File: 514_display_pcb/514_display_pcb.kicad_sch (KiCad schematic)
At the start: 9 parts

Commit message: Initial commit from workspace
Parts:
- U?: footprint XIAO_ESP32C3:xiao_esp32c3 -> RF_Module:MCU_Seeed_ESP32C3
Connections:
- net at Lipo?.1 (+): now also U?.1 (VI), U?.3 (VIN1+)
- net at D?.2 (GND): now also Brd?.1 (GND), SW?.1, U?.13 (GND)
- net at D?.3 (VDD): now also Brd?.2 (VCC), U?.12 (VCC_3V3)
- net at D?.4 (DIN): now also U?.2 (D1)
- net at SW?.2: now also U?.7 (D6)
- net at U?.5 (VOUT1-): now also U?.8 (GND)
- net at U?.7 (VOUT1+): now also U?.9 (COM)
- net at U?.5 (D4): now also Brd?.4 (SDA)
- net at U?.6 (D5): now also Brd?.3 (SCL)
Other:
- moved on the sheet: D?, SW?, U?

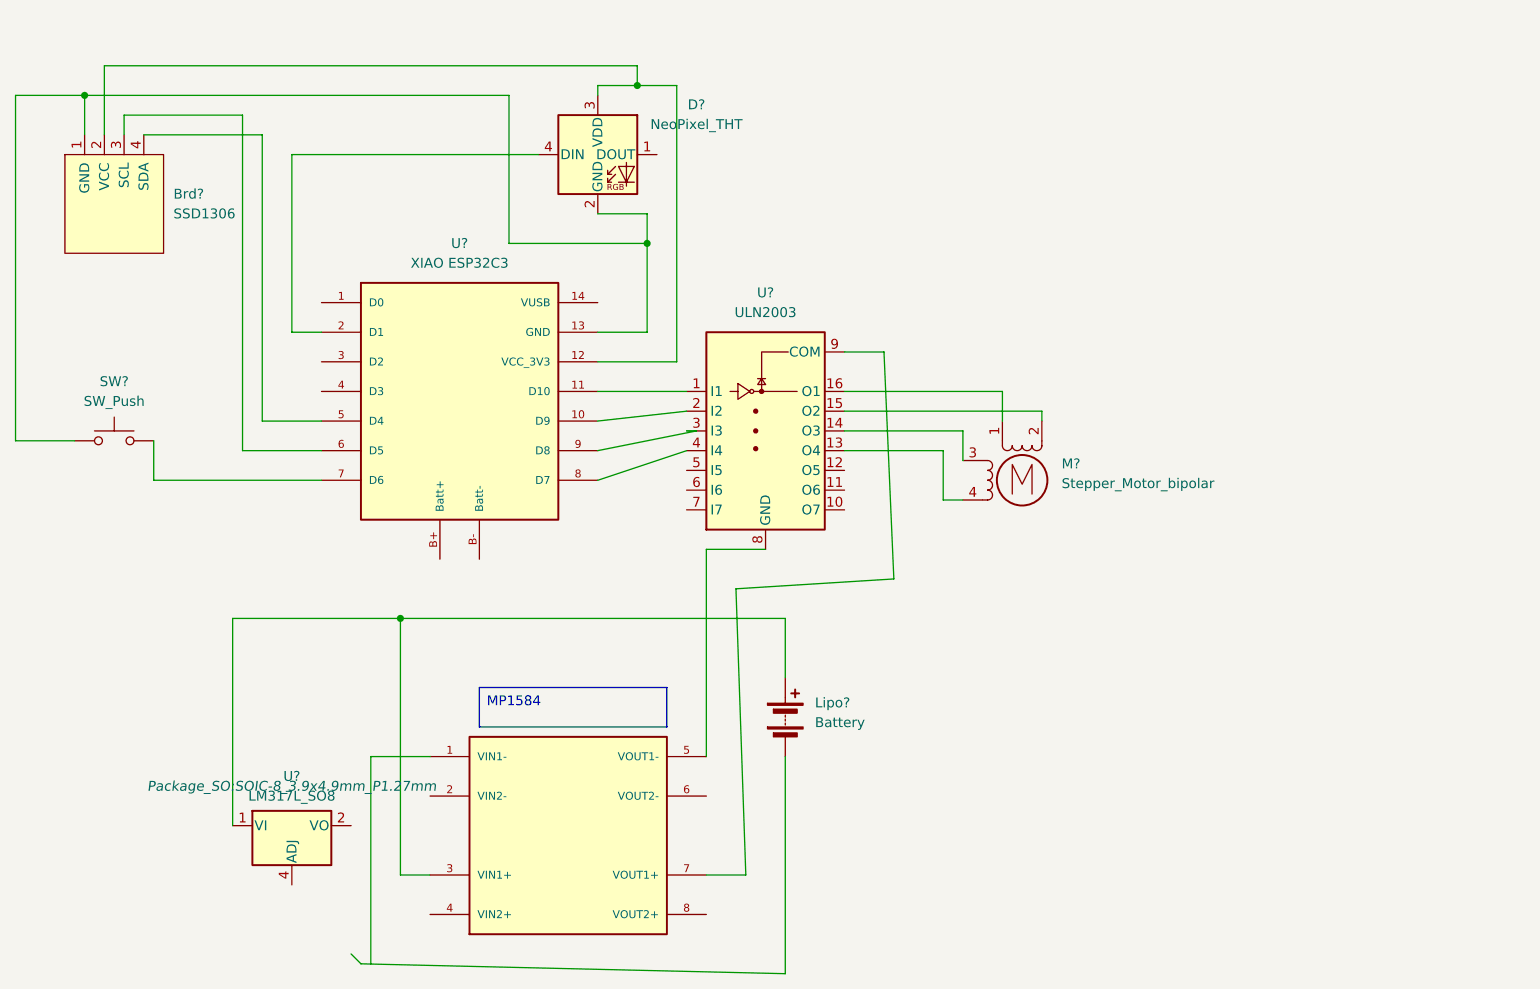
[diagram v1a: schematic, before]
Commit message: Update project files - Add 514_code, sensor/display PCB updates, enclosure folder, and additional resources
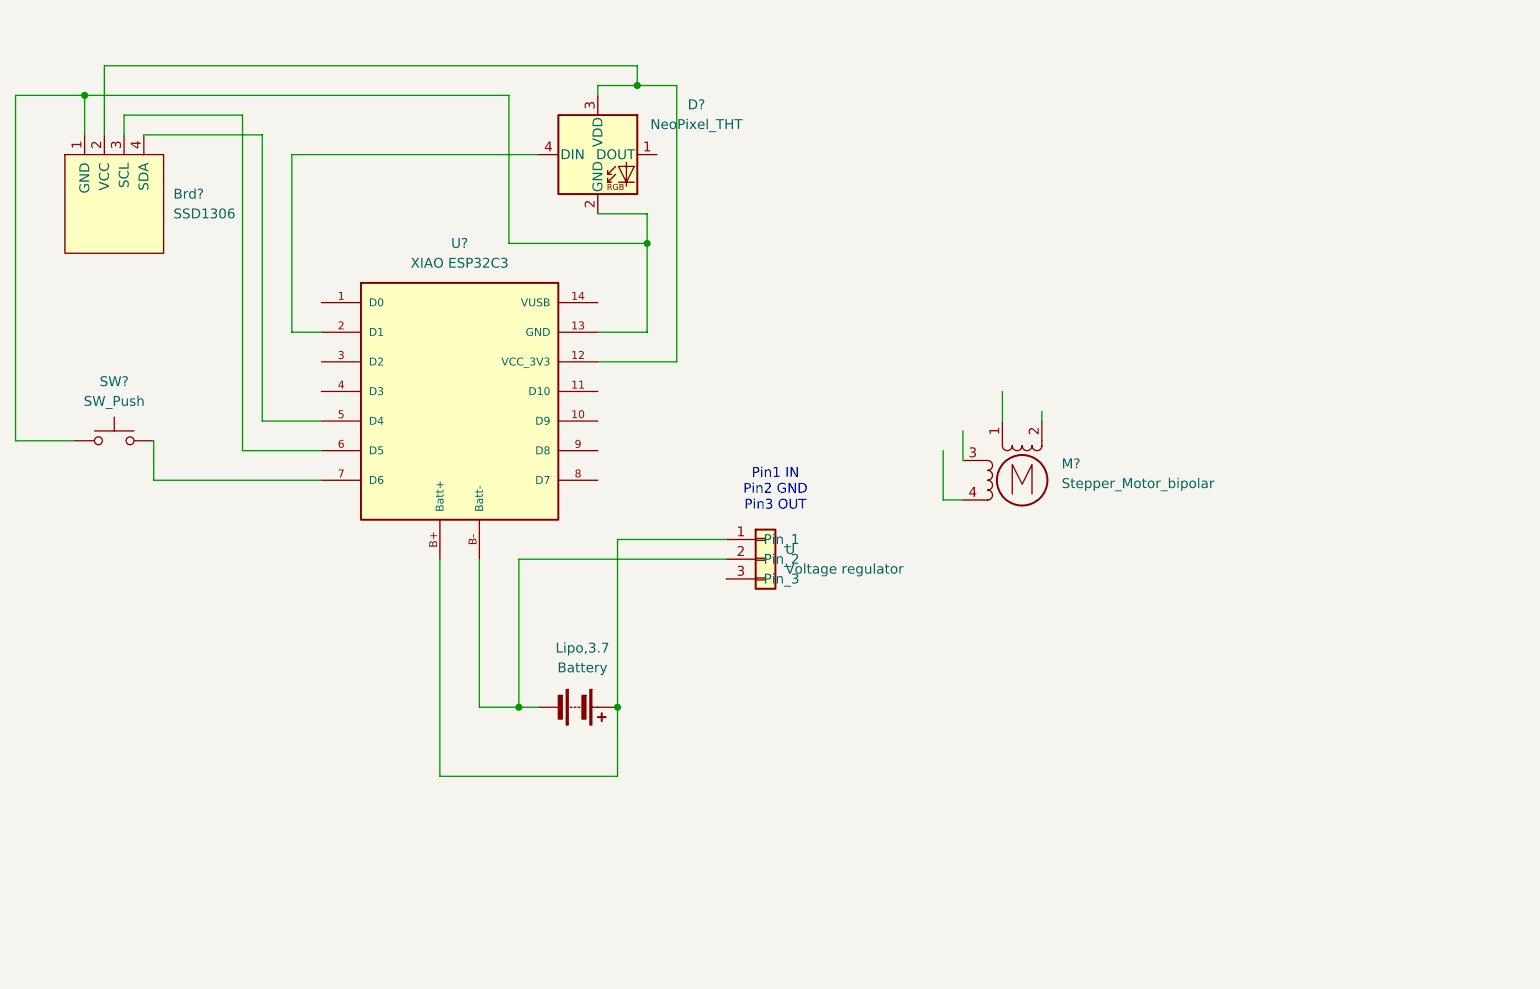
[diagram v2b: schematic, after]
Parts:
- removed U?: LM317L_SO8, Package_SO:SOIC-8_3.9x4.9mm_P1.27mm, symbol Regulator_Linear:LM317L_SO8
- removed U?: MP1584, MP1584_AMAZON, symbol Regulator_Linear:MP1584
- removed U?: ULN2003, symbol Transistor_Array:ULN2003
- added U: Voltage regulator, symbol Connector_Generic:Conn_01x03
- gave numbers to parts that had none: 1
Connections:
- net at Lipo,3.7.1 (+): now also U?.B+ (Batt+), U.1 (Pin_1)
- net at Lipo,3.7.2 (-): now also U?.B- (Batt-), U.2 (Pin_2)
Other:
- note added: "Pin1 IN Pin2 GND Pin3 OUT"
- moved on the sheet: Lipo,3.7
